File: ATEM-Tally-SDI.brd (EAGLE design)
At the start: 106 x 100 mm, 11 parts

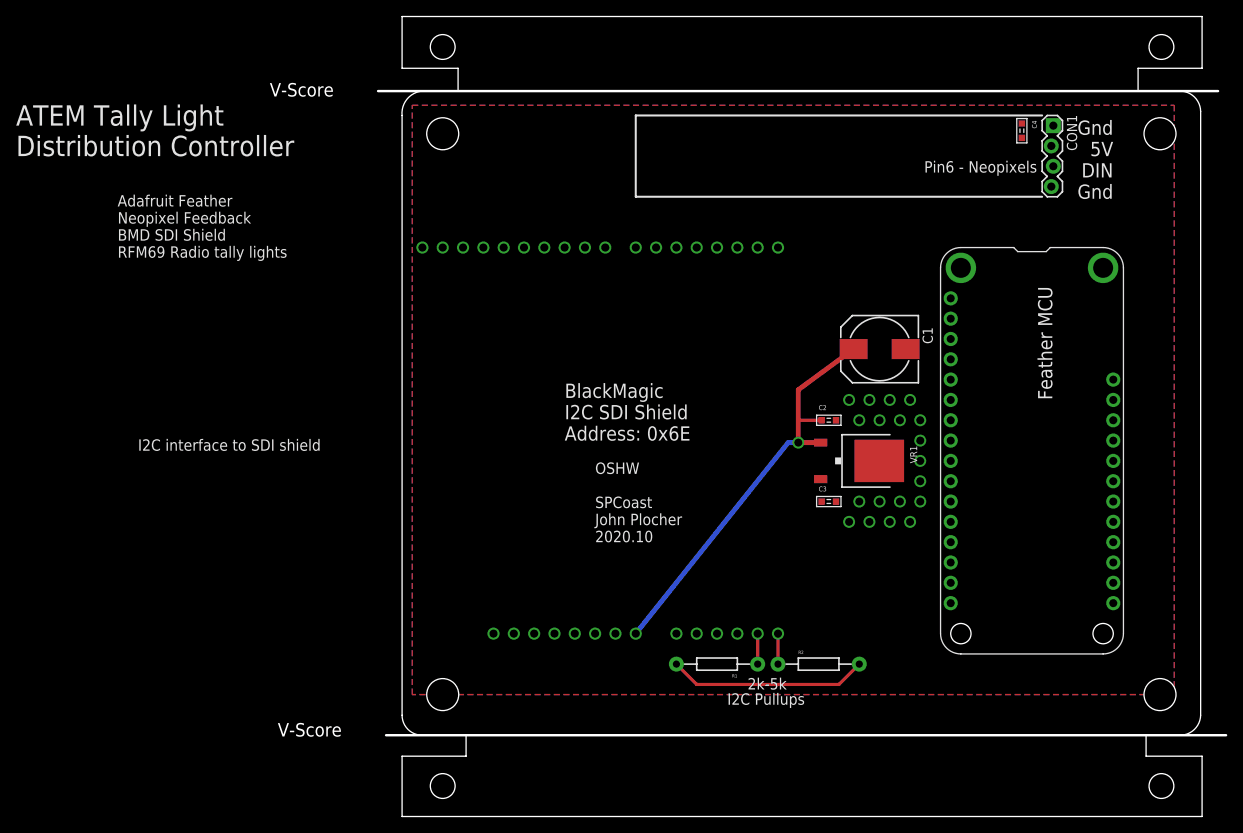
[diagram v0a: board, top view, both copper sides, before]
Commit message: fixed airwires
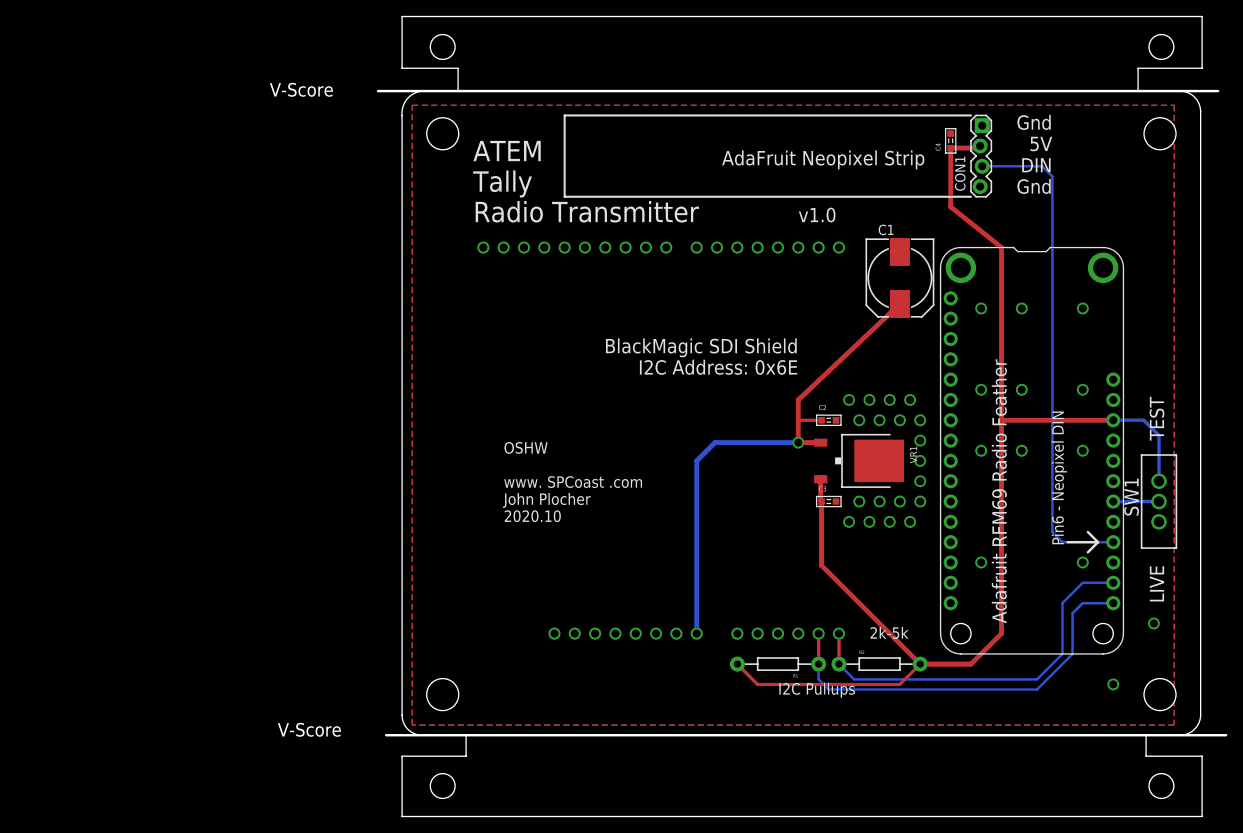
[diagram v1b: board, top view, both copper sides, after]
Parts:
- added SW1: (no value), SPCoast:SWITCH-SPDT
- moved C1 9.25 mm to (62.2, 67.3), turned to 270 degrees
- moved C4 8.98 mm to (68.6, 84.5), turned to 90 degrees
- moved CON1 8.89 mm to (72.4, 86.4)
- moved R1 7.62 mm to (47.0, 19.1)
- moved SDISHIELD 7.62 mm to (8.89, 72.4)
- moved R2 7.62 mm to (59.7, 19.1)
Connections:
- new net TEST: FEATHER.22, SW1.2
- net 5V: now also SW1.1
- net GND: now also FEATHER.21, SW1.3
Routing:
- net 5V: track 25.0 -> 158.7 mm
- net NEOPIXEL: track 0.00 -> 61.9 mm
- net SDA: track 3.81 -> 50.5 mm
- net SCL: track 3.81 -> 47.6 mm
- net VIN: track 52.7 -> 63.7 mm
- net TEST: track 0.00 -> 5.71 mm
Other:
- board text added: "ATEM Tally Radio Transmitter"
- board text added: "AdaFruit Neopixel Strip"
- board text added: "Adafruit RFM69 Radio Feather"
- board text added: "BlackMagic SDI Shield I2C Address: 0x6E"
- board text added: "LIVE"
- board text added: "OSHW www. SPCoast .com John Plocher 2020.10"
- board text added: "Pin6 - Neopixel DIN"
- board text added: "TEST"
- board text added: "v1.0"
- board text removed: "ATEM Tally Light Distribution Controller"
- board text removed: "Adafruit Feather Neopixel Feedback BMD SDI Shield RFM69 Radio tally lights"
- board text removed: "BlackMagic I2C SDI Shield Address: 0x6E"
- board text removed: "Feather MCU"
- board text removed: "I2C interface to SDI shield"
- board text removed: "OSHW SPCoast John Plocher 2020.10"
- board text removed: "Pin6 - Neopixels"

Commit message: Moved Feather to make room for antenna
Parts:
- moved FEATHER 3.81 mm to (67.3, 74.9)
- moved SW1 3.81 mm to (94.6, 43.2)
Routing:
- net SDA: track 50.5 -> 54.3 mm
- net SCL: track 47.6 -> 51.4 mm
- net NEOPIXEL: track 61.9 -> 58.1 mm
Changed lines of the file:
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@@
 Tally
 Radio Transmitter </text>
-<text x="75.565" y="24.13" size="1.778" layer="21" font="vector" ratio="15" rot="R90">Adafruit RFM69 Radio Feather</text>
+<text x="75.565" y="27.94" size="1.778" layer="21" font="vector" ratio="15" rot="R90">Adafruit RFM69 Radio Feather</text>
 <text x="12.7" y="36.83" size="1.4224" layer="21" font="vector" ratio="15">OSHW
 www. SPCoast .com
@@
 2020.10</text>
 <text x="46.99" y="15.24" size="1.4224" layer="21" font="vector" ratio="15">I2C Pullups</text>
-<text x="81.28" y="50.8" size="1.4224" layer="21" font="vector" ratio="15" rot="R270">Pin6 - Neopixel DIN</text>
+<text x="81.28" y="54.61" size="1.4224" layer="21" font="vector" ratio="15" rot="R270">Pin6 - Neopixel DIN</text>
 <text x="58.42" y="22.225" size="1.4224" layer="21" font="vector" ratio="15">2k-5k</text>
 <wire x1="20.32" y1="77.47" x2="71.12" y2="77.47" width="0.254" layer="21"/>
 <wire x1="20.32" y1="87.63" x2="71.12" y2="87.63" width="0.254" layer="21"/>
 <wire x1="20.32" y1="77.47" x2="20.32" y2="87.63" width="0.254" layer="21"/>
-<text x="95.25" y="46.99" size="1.778" layer="21" font="vector" ratio="10" rot="R90">TEST</text>
-<text x="95.25" y="26.67" size="1.778" layer="21" font="vector" ratio="10" rot="R90">LIVE</text>
+<text x="95.25" y="50.8" size="1.778" layer="21" font="vector" ratio="10" rot="R90">TEST</text>
+<text x="95.25" y="30.48" size="1.778" layer="21" font="vector" ratio="10" rot="R90">LIVE</text>
 <text x="65.405" y="83.185" size="1.778" layer="21" font="vector" ratio="15" rot="R180">AdaFruit Neopixel Strip</text>
-<wire x1="83.185" y1="34.29" x2="86.995" y2="34.29" width="0.3048" layer="21"/>
-<wire x1="86.995" y1="34.29" x2="85.725" y2="35.56" width="0.3048" layer="21"/>
-<wire x1="86.995" y1="34.29" x2="85.725" y2="33.02" width="0.3048" layer="21"/>
+<wire x1="83.185" y1="38.1" x2="86.995" y2="38.1" width="0.3048" layer="21"/>
+<wire x1="86.995" y1="38.1" x2="85.725" y2="39.37" width="0.3048" layer="21"/>
+<wire x1="86.995" y1="38.1" x2="85.725" y2="36.83" width="0.3048" layer="21"/>
 <text x="49.53" y="74.295" size="1.778" layer="21" font="vector">v1.0</text>
 </plain>
@@
 <attribute name="VALUE" x="69.215" y="87.63" size="1.27" layer="27" rot="R270"/>
 </element>
-<element name="FEATHER" library="adafruit" package="FEATHERWING_DIM" value="FEATHERWING_NODIM" x="67.31" y="71.12" rot="R270"/>
+<element name="FEATHER" library="adafruit" package="FEATHERWING_DIM" value="FEATHERWING_NODIM" x="67.31" y="74.93" rot="R270"/>
 <element name="VR1" library="SPCoast" package="TO-252" value="" x="57.15" y="44.45"/>
 <element name="BOARD1" library="SPCoast" package="BOARD-DINRAIL-3.17INX10CM" value="" x="0" y="0"/>
 <element name="R1" library="SPCoast" package="AXIAL-0.4-RES" value="" x="46.99" y="19.05" rot="R180"/>
 <element name="R2" library="SPCoast" package="AXIAL-0.4-RES" value="" x="59.69" y="19.05"/>
-<element name="SW1" library="SPCoast" package="SWITCH-SPDT" value="" x="94.615" y="39.37" smashed="yes">
-<attribute name="NAME" x="92.075" y="37.465" size="1.778" layer="25" font="vector" ratio="10" rot="R90"/>
-<attribute name="VALUE" x="90.805" y="29.845" size="1.778" layer="27" ratio="10"/>
+<element name="SW1" library="SPCoast" package="SWITCH-SPDT" value="" x="94.615" y="43.18" smashed="yes">
+<attribute name="NAME" x="92.075" y="41.275" size="1.778" layer="25" font="vector" ratio="10" rot="R90"/>
+<attribute name="VALUE" x="90.805" y="33.655" size="1.778" layer="27" ratio="10"/>
 </element>
 </elements>
@@
 <contactref element="R1" pad="P$1"/>
 <wire x1="52.07" y1="19.05" x2="52.07" y2="22.86" width="0.4064" layer="1"/>
-<wire x1="88.9" y1="26.67" x2="85.09" y2="26.67" width="0.3048" layer="16"/>
-<wire x1="85.09" y1="26.67" x2="83.82" y2="25.4" width="0.3048" layer="16"/>
-<wire x1="83.82" y1="25.4" x2="83.82" y2="20.32" width="0.3048" layer="16"/>
+<wire x1="88.9" y1="30.48" x2="85.09" y2="30.48" width="0.3048" layer="16"/>
+<wire x1="85.09" y1="30.48" x2="83.82" y2="29.21" width="0.3048" layer="16"/>
+<wire x1="83.82" y1="29.21" x2="83.82" y2="20.32" width="0.3048" layer="16"/>
 <wire x1="83.82" y1="20.32" x2="79.375" y2="15.875" width="0.3048" layer="16"/>
 <wire x1="79.375" y1="15.875" x2="53.34" y2="15.875" width="0.3048" layer="16"/>
@@
 <contactref element="R2" pad="P$1"/>
 <wire x1="54.61" y1="19.05" x2="54.61" y2="22.86" width="0.4064" layer="1"/>
-<wire x1="88.9" y1="29.21" x2="85.09" y2="29.21" width="0.3048" layer="16"/>
-<wire x1="85.09" y1="29.21" x2="82.55" y2="26.67" width="0.3048" layer="16"/>
-<wire x1="82.55" y1="26.67" x2="82.55" y2="20.32" width="0.3048" layer="16"/>
+<wire x1="88.9" y1="33.02" x2="85.09" y2="33.02" width="0.3048" layer="16"/>
+<wire x1="85.09" y1="33.02" x2="82.55" y2="30.48" width="0.3048" layer="16"/>
+<wire x1="82.55" y1="30.48" x2="82.55" y2="20.32" width="0.3048" layer="16"/>
 <wire x1="82.55" y1="20.32" x2="79.375" y2="17.145" width="0.3048" layer="16"/>
 <wire x1="79.375" y1="17.145" x2="56.515" y2="17.145" width="0.3048" layer="16"/>
@@
 <contactref element="C3" pad="2"/>
 <contactref element="C4" pad="2"/>
-<polygon width="0.4064" layer="1" isolate="0.4064">
+<polygon width="0.3048" layer="1" isolate="0.4064">
 <vertex x="1.27" y="88.9"/>
 <vertex x="96.52" y="88.9"/>
@@
 <via x="58.42" y="52.07" extent="1-16" drill="1"/>
 <via x="55.88" y="52.07" extent="1-16" drill="1"/>
-<polygon width="0.4064" layer="16" isolate="0.4064">
+<polygon width="0.3048" layer="16" isolate="0.4064">
 <vertex x="1.27" y="88.9"/>
 <vertex x="96.52" y="88.9"/>
@@
 <contactref element="SW1" pad="3"/>
 <contactref element="FEATHER" pad="21"/>
-<via x="85.09" y="45.72" extent="1-16" drill="1"/>
-<via x="85.09" y="31.75" extent="1-16" drill="1"/>
-<via x="85.09" y="53.34" extent="1-16" drill="1"/>
-<via x="85.09" y="63.5" extent="1-16" drill="1"/>
-<via x="77.47" y="53.34" extent="1-16" drill="1"/>
-<via x="77.47" y="63.5" extent="1-16" drill="1"/>
-<via x="77.47" y="45.72" extent="1-16" drill="1"/>
+<via x="85.09" y="49.53" extent="1-16" drill="1"/>
+<via x="85.09" y="35.56" extent="1-16" drill="1"/>
+<via x="85.09" y="57.15" extent="1-16" drill="1"/>
+<via x="85.09" y="67.31" extent="1-16" drill="1"/>
+<via x="77.47" y="57.15" extent="1-16" drill="1"/>
+<via x="77.47" y="67.31" extent="1-16" drill="1"/>
+<via x="77.47" y="49.53" extent="1-16" drill="1"/>
 <via x="93.98" y="24.13" extent="1-16" drill="1"/>
 <via x="88.9" y="16.51" extent="1-16" drill="1"/>
-<via x="72.39" y="63.5" extent="1-16" drill="1"/>
-<via x="72.39" y="53.34" extent="1-16" drill="1"/>
-<via x="72.39" y="45.72" extent="1-16" drill="1"/>
-<via x="72.39" y="31.75" extent="1-16" drill="1"/>
+<via x="72.39" y="67.31" extent="1-16" drill="1"/>
+<via x="72.39" y="57.15" extent="1-16" drill="1"/>
+<via x="72.39" y="49.53" extent="1-16" drill="1"/>
+<via x="72.39" y="35.56" extent="1-16" drill="1"/>
 </signal>
 <signal name="5V">
@@
 <wire x1="62.23" y1="16.51" x2="64.77" y2="19.05" width="0.4064" layer="1"/>
 <contactref element="SW1" pad="1"/>
-<wire x1="94.615" y1="41.91" x2="94.615" y2="47.625" width="0.4064" layer="16"/>
-<wire x1="94.615" y1="47.625" x2="92.71" y2="49.53" width="0.4064" layer="16"/>
-<wire x1="92.71" y1="49.53" x2="88.9" y2="49.53" width="0.4064" layer="16"/>
+<wire x1="94.615" y1="45.72" x2="94.615" y2="51.435" width="0.4064" layer="16"/>
+<wire x1="94.615" y1="51.435" x2="92.71" y2="53.34" width="0.4064" layer="16"/>
+<wire x1="92.71" y1="53.34" x2="88.9" y2="53.34" width="0.4064" layer="16"/>
 <wire x1="52.324" y1="42.164" x2="52.324" y2="39.486" width="0.6096" layer="1"/>
 <wire x1="52.324" y1="39.486" x2="52.44" y2="39.37" width="0.6096" layer="1"/>
 <wire x1="52.44" y1="39.37" x2="52.44" y2="31.38" width="0.6096" layer="1"/>
 <wire x1="52.44" y1="31.38" x2="64.77" y2="19.05" width="0.6096" layer="1"/>
-<wire x1="88.9" y1="49.53" x2="74.93" y2="49.53" width="0.6096" layer="1"/>
-<wire x1="74.93" y1="49.53" x2="74.93" y2="22.86" width="0.6096" layer="1"/>
+<wire x1="88.9" y1="53.34" x2="74.93" y2="53.34" width="0.6096" layer="1"/>
+<wire x1="74.93" y1="53.34" x2="74.93" y2="22.86" width="0.6096" layer="1"/>
 <wire x1="74.93" y1="22.86" x2="71.12" y2="19.05" width="0.6096" layer="1"/>
 <wire x1="71.12" y1="19.05" x2="64.77" y2="19.05" width="0.6096" layer="1"/>
 <wire x1="68.58" y1="83.555" x2="71.998" y2="83.555" width="0.6096" layer="1"/>
 <wire x1="71.998" y1="83.555" x2="72.263" y2="83.82" width="0.3048" layer="1"/>
-<wire x1="74.93" y1="49.53" x2="74.93" y2="71.12" width="0.6096" layer="1"/>
-<wire x1="74.93" y1="71.12" x2="68.58" y2="76.2" width="0.6096" layer="1"/>
-<wire x1="68.58" y1="76.2" x2="68.58" y2="83.555" width="0.6096" layer="1"/>
+<wire x1="74.93" y1="53.34" x2="74.93" y2="73.66" width="0.6096" layer="1"/>
+<wire x1="74.93" y1="73.66" x2="68.58" y2="78.74" width="0.6096" layer="1"/>
+<wire x1="68.58" y1="78.74" x2="68.58" y2="83.555" width="0.6096" layer="1"/>
 </signal>
 <signal name="NEOPIXEL">
 <contactref element="FEATHER" pad="20"/>
 <contactref element="CON1" pad="3"/>
-<wire x1="81.28" y1="80.01" x2="81.28" y2="35.56" width="0.3048" layer="16"/>
-<wire x1="81.28" y1="35.56" x2="82.55" y2="34.29" width="0.3048" layer="16"/>
-<wire x1="82.55" y1="34.29" x2="88.9" y2="34.29" width="0.3048" layer="16"/>
+<wire x1="81.28" y1="80.01" x2="81.28" y2="39.37" width="0.3048" layer="16"/>
+<wire x1="81.28" y1="39.37" x2="82.55" y2="38.1" width="0.3048" layer="16"/>
+<wire x1="82.55" y1="38.1" x2="88.9" y2="38.1" width="0.3048" layer="16"/>
 <wire x1="81.28" y1="80.01" x2="80.01" y2="81.28" width="0.3048" layer="16"/>
 <wire x1="80.01" y1="81.28" x2="72.517" y2="81.28" width="0.3048" layer="16"/>
@@
 <contactref element="FEATHER" pad="22"/>
 <contactref element="SW1" pad="2"/>
-<wire x1="94.615" y1="39.37" x2="88.9" y2="39.37" width="0.4064" layer="16"/>
+<wire x1="94.615" y1="43.18" x2="88.9" y2="43.18" width="0.4064" layer="16"/>
 </signal>
 </signals>

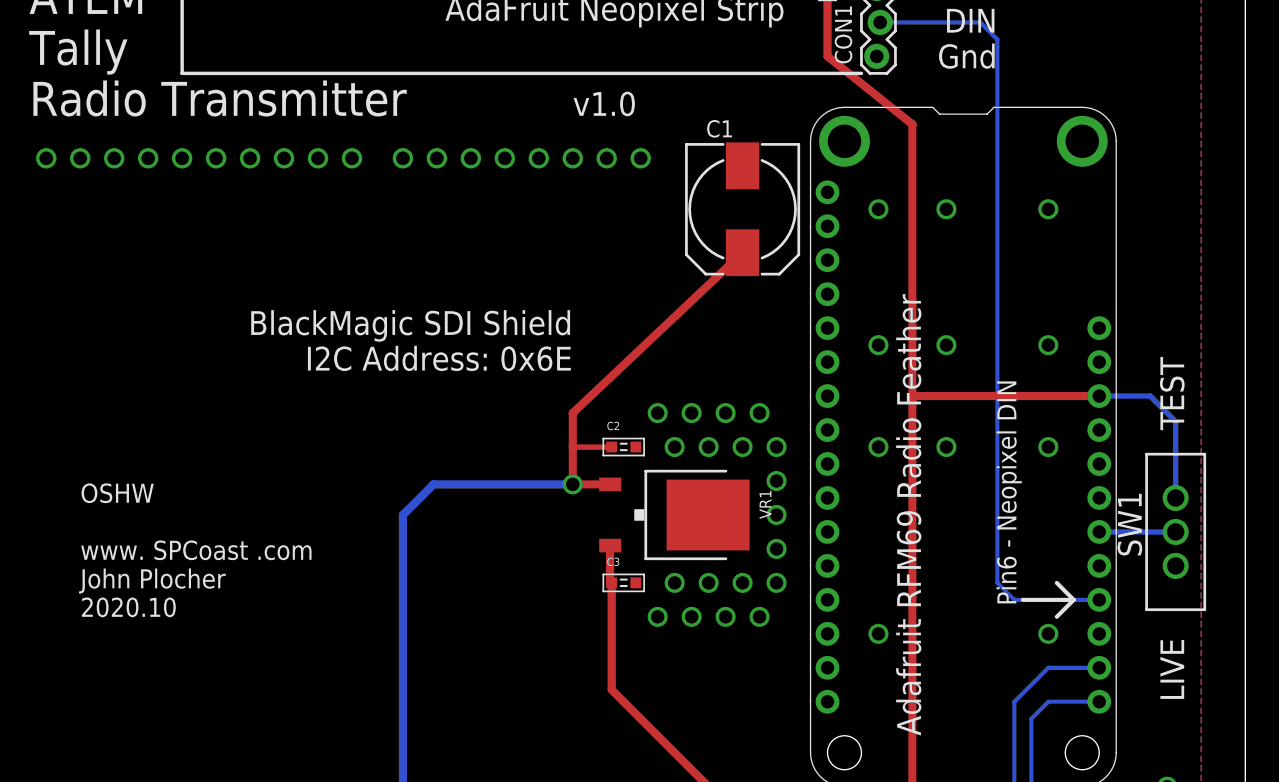
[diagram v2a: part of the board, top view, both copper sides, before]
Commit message: revamped options pins
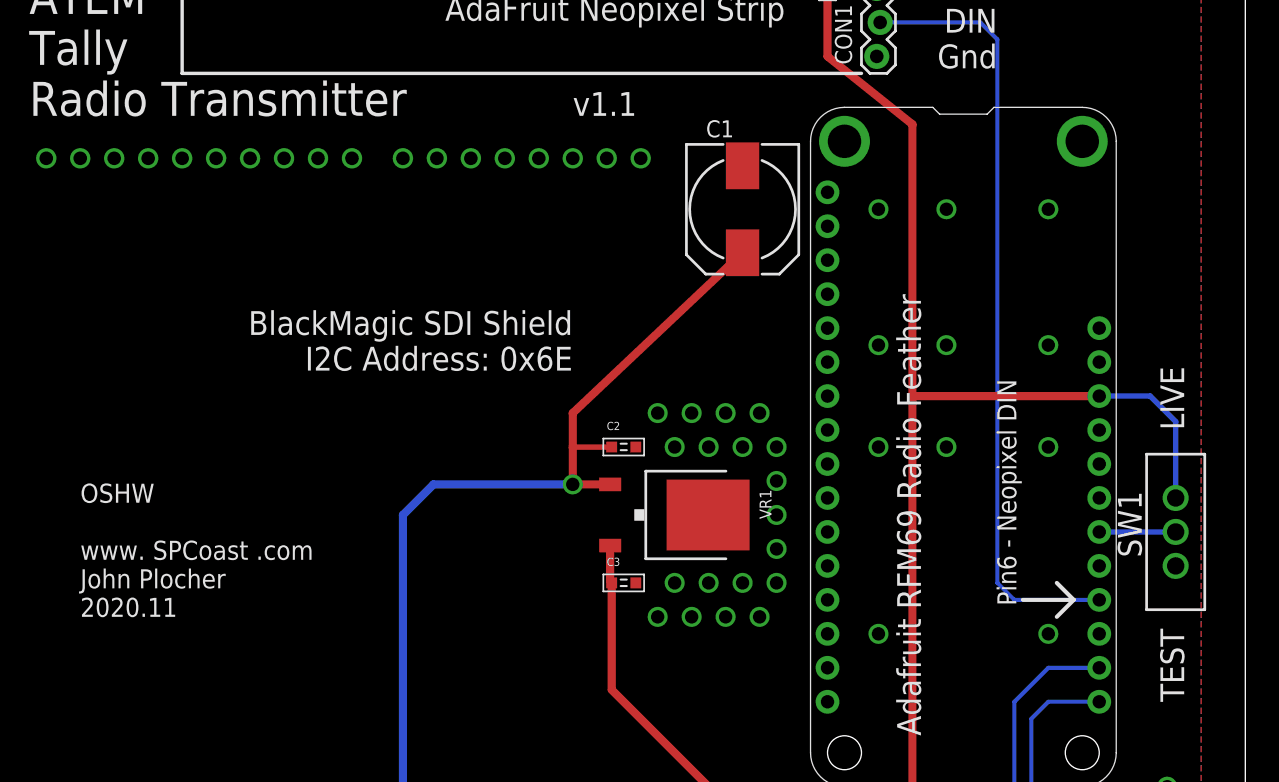
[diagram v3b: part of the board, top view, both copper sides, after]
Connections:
- net TEST renamed !TEST
- net GND: now also FEATHER.23, FEATHER.24
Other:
- board text added: "OSHW www. SPCoast .com John Plocher 2020.11"
- board text added: "v1.1"
- board text removed: "OSHW www. SPCoast .com John Plocher 2020.10"
- board text removed: "v1.0"
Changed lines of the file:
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@@
 www. SPCoast .com
 John Plocher
-2020.10</text>
+2020.11</text>
 <text x="46.99" y="15.24" size="1.4224" layer="21" font="vector" ratio="15">I2C Pullups</text>
 <text x="81.28" y="54.61" size="1.4224" layer="21" font="vector" ratio="15" rot="R270">Pin6 - Neopixel DIN</text>
@@
 <wire x1="20.32" y1="87.63" x2="71.12" y2="87.63" width="0.254" layer="21"/>
 <wire x1="20.32" y1="77.47" x2="20.32" y2="87.63" width="0.254" layer="21"/>
-<text x="95.25" y="50.8" size="1.778" layer="21" font="vector" ratio="10" rot="R90">TEST</text>
-<text x="95.25" y="30.48" size="1.778" layer="21" font="vector" ratio="10" rot="R90">LIVE</text>
+<text x="95.25" y="30.48" size="1.778" layer="21" font="vector" ratio="10" rot="R90">TEST</text>
+<text x="95.25" y="50.8" size="1.778" layer="21" font="vector" ratio="10" rot="R90">LIVE</text>
 <text x="65.405" y="83.185" size="1.778" layer="21" font="vector" ratio="15" rot="R180">AdaFruit Neopixel Strip</text>
 <wire x1="83.185" y1="38.1" x2="86.995" y2="38.1" width="0.3048" layer="21"/>
 <wire x1="86.995" y1="38.1" x2="85.725" y2="39.37" width="0.3048" layer="21"/>
 <wire x1="86.995" y1="38.1" x2="85.725" y2="36.83" width="0.3048" layer="21"/>
-<text x="49.53" y="74.295" size="1.778" layer="21" font="vector">v1.0</text>
+<text x="49.53" y="74.295" size="1.778" layer="21" font="vector">v1.1</text>
 </plain>
 <attributes>
@@
 <via x="72.39" y="49.53" extent="1-16" drill="1"/>
 <via x="72.39" y="35.56" extent="1-16" drill="1"/>
+<contactref element="FEATHER" pad="23"/>
+<contactref element="FEATHER" pad="24"/>
+<wire x1="88.9" y1="45.72" x2="88.9" y2="48.26" width="0" layer="19" extent="1-1"/>
+<wire x1="85.09" y1="49.53" x2="88.9" y2="48.26" width="0" layer="19" extent="1-1"/>
 </signal>
 <signal name="5V">
@@
 <wire x1="80.01" y1="81.28" x2="72.517" y2="81.28" width="0.3048" layer="16"/>
 </signal>
-<signal name="TEST">
+<signal name="!TEST">
 <contactref element="FEATHER" pad="22"/>
 <contactref element="SW1" pad="2"/>
